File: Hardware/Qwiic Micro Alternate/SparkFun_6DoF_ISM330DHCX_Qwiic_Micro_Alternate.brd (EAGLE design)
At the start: 19.1 x 7.6 mm, 38 parts, among them J1 Qwiic Right Angle, U1 ISM330DHCX

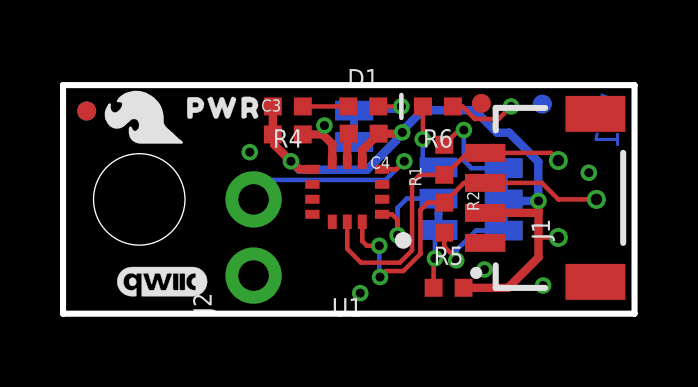
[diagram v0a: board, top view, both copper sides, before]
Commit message: Removes unused size
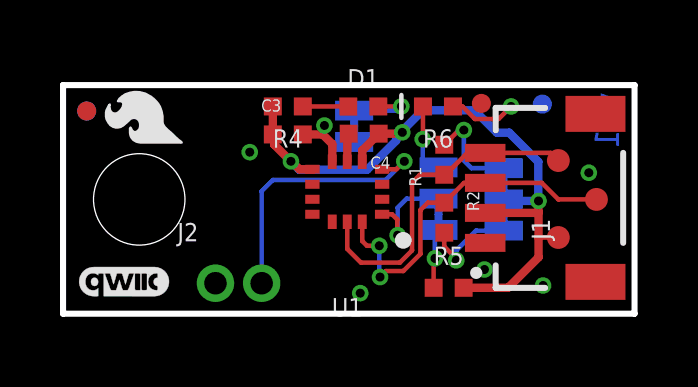
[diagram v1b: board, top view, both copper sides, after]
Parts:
- removed U$28: (no value), top:PWR8
- J2: device SparkFun-Connectors:1X02_NO_SILK -> SparkFun-Connectors:1X02_1.5MM_NO_SILK
- TP1, TP2, TP3: value TEST-POINTTP_15TH_THRU -> TEST-POINT3; device SparkFun-Connectors:TP_15TH -> SparkFun-Connectors:PAD.03X.03
- moved J2 1.30 mm to (5.08, 1.02), turned to 0 degrees
- moved LOGO1 1.27 mm to (2.03, 1.07)
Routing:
- net INT1: track 6.40 -> 9.08 mm
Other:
- board text removed: "Units in Inches"
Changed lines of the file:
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@@
 <drawing>
 <settings>
-<setting alwaysvectorfont="no"/>
+<setting alwaysvectorfont="yes"/>
 <setting keepoldvectorfont="yes"/>
 <setting verticaltext="up"/>
 </settings>
-<grid distance="0.05" unitdist="inch" unit="inch" style="dots" multiple="1" display="yes" altdistance="0.005" altunitdist="inch" altunit="inch"/>
+<grid distance="0.02" unitdist="inch" unit="inch" style="dots" multiple="1" display="yes" altdistance="0.005" altunitdist="inch" altunit="inch"/>
 <layers>
-<layer number="1" name="Top" color="4" fill="1" visible="yes" active="yes"/>
+<layer number="1" name="Top" color="4" fill="1" visible="no" active="yes"/>
 <layer number="2" name="Route2" color="1" fill="3" visible="no" active="no"/>
 <layer number="3" name="Route3" color="4" fill="3" visible="no" active="no"/>
@@
 <layer number="14" name="Route14" color="1" fill="6" visible="no" active="no"/>
 <layer number="15" name="Route15" color="4" fill="6" visible="no" active="no"/>
-<layer number="16" name="Bottom" color="3" fill="1" visible="yes" active="yes"/>
+<layer number="16" name="Bottom" color="3" fill="1" visible="no" active="yes"/>
 <layer number="17" name="Pads" color="26" fill="1" visible="yes" active="yes"/>
-<layer number="18" name="Vias" color="2" fill="1" visible="yes" active="yes"/>
+<layer number="18" name="Vias" color="2" fill="1" visible="no" active="yes"/>
 <layer number="19" name="Unrouted" color="6" fill="1" visible="yes" active="yes"/>
 <layer number="20" name="Dimension" color="15" fill="1" visible="yes" active="yes"/>
 <layer number="21" name="tPlace" color="16" fill="1" visible="yes" active="yes"/>
-<layer number="22" name="bPlace" color="14" fill="1" visible="yes" active="yes"/>
+<layer number="22" name="bPlace" color="14" fill="1" visible="no" active="yes"/>
 <layer number="23" name="tOrigins" color="15" fill="1" visible="yes" active="yes"/>
 <layer number="24" name="bOrigins" color="15" fill="1" visible="yes" active="yes"/>
@@
 <layer number="29" name="tStop" color="7" fill="3" visible="no" active="yes"/>
 <layer number="30" name="bStop" color="7" fill="6" visible="no" active="yes"/>
-<layer number="31" name="tCream" color="7" fill="4" visible="no" active="yes"/>
+<layer number="31" name="tCream" color="7" fill="4" visible="yes" active="yes"/>
 <layer number="32" name="bCream" color="7" fill="5" visible="no" active="yes"/>
 <layer number="33" name="tFinish" color="6" fill="3" visible="no" active="yes"/>
@@
 <layer number="37" name="tTest" color="7" fill="1" visible="no" active="yes"/>
 <layer number="38" name="bTest" color="7" fill="1" visible="no" active="yes"/>
-<layer number="39" name="tKeepout" color="4" fill="11" visible="no" active="yes"/>
+<layer number="39" name="tKeepout" color="4" fill="11" visible="yes" active="yes"/>
 <layer number="40" name="bKeepout" color="1" fill="11" visible="no" active="yes"/>
 <layer number="41" name="tRestrict" color="4" fill="10" visible="no" active="yes"/>
@@
 <layer number="45" name="Holes" color="7" fill="1" visible="yes" active="yes"/>
 <layer number="46" name="Milling" color="3" fill="1" visible="no" active="yes"/>
-<layer number="47" name="Measures" color="7" fill="1" visible="no" active="yes"/>
+<layer number="47" name="Measures" color="7" fill="1" visible="yes" active="yes"/>
 <layer number="48" name="Document" color="7" fill="1" visible="no" active="yes"/>
 <layer number="49" name="Reference" color="13" fill="1" visible="yes" active="yes"/>
 <layer number="50" name="dxf" color="7" fill="1" visible="no" active="no"/>
-<layer number="51" name="tDocu" color="6" fill="1" visible="yes" active="yes"/>
+<layer number="51" name="tDocu" color="6" fill="1" visible="no" active="yes"/>
 <layer number="52" name="bDocu" color="7" fill="1" visible="no" active="yes"/>
 <layer number="53" name="tGND_GNDA" color="7" fill="9" visible="no" active="no"/>
@@
 <text x="18.532475" y="7.375525" size="0.8128" layer="16" font="vector" ratio="22" rot="SMR270">v01</text>
 <dimension x1="14.0716" y1="3.8608" x2="13.97" y2="0" x3="22.86" y3="1.9304" textsize="1.778" textratio="15" layer="47" dtype="vertical" unit="inch"/>
-<text x="-1.27" y="-3.81" size="1.778" layer="47" font="vector" ratio="15">Units in Inches</text>
 <rectangle x1="9.1948" y1="4.953" x2="9.2456" y2="5.1816" layer="41"/>
 <dimension x1="19.05" y1="8.89" x2="0" y2="8.89" x3="9.525" y3="15.24" textsize="1.778" layer="47" dtype="horizontal" unit="inch"/>
 <dimension x1="2.54" y1="3.81" x2="0" y2="3.81" x3="1.27" y3="11.43" textsize="1.778" layer="47" dtype="horizontal" unit="inch"/>
-<dimension x1="0" y1="8.89" x2="0" y2="0" x3="-11.43" y3="4.445" textsize="1.778" layer="47" dtype="horizontal" unit="inch"/>
 <wire x1="18.542" y1="6.353175" x2="16.637" y2="6.353175" width="0.254" layer="22"/>
 <wire x1="17.145" y1="5.845175" x2="17.145" y2="6.988175" width="0.254" layer="22" curve="180"/>
@@
 <wire x1="3.190875" y1="7.24535" x2="2.784475" y2="5.63245" width="0.254" layer="22" curve="100"/>
 <circle x="3.6449" y="6.28015" radius="0.5334" width="0.254" layer="22"/>
-<dimension x1="2.54" y1="3.81" x2="2.54" y2="0" x3="-6.35" y3="1.905" textsize="1.778" layer="47" unit="inch"/>
 <wire x1="4.064" y1="5.842" x2="3.175" y2="6.731" width="0.254" layer="22"/>
 <wire x1="3.302" y1="5.842" x2="4.191" y2="6.731" width="0.254" layer="22"/>
+<dimension x1="0" y1="7.62" x2="0" y2="0" x3="-5.08" y3="3.81" textsize="1.778" layer="47" unit="inch"/>
 </plain>
 <attributes>
@@
 </element>
 <element name="U$25" library="bot" package="#I2C#11" value="" x="16.2814" y="3.8862" smashed="yes" rot="MR90"/>
-<element name="U$28" library="top" package="PWR8" value="" x="5.3594" y="6.858" smashed="yes"/>
 <element name="R5" library="SparkFun-Resistors" package="0402-TIGHT" value="10k" x="12.8524" y="0.8636" smashed="yes">
 <attribute name="NAME" x="12.8524" y="1.6256" size="0.6096" layer="25" font="vector" ratio="20" align="bottom-center"/>
@@
 <attribute name="VALUE" x="17.3736" y="2.2098" size="0.6096" layer="27" font="vector" ratio="20" rot="R90"/>
 </element>
-<element name="LOGO1" library="SparkFun-Aesthetics" package="QWIIC_3MM" value="QWIIC_LOGO_3MM" x="3.302" y="1.0668" smashed="yes"/>
+<element name="LOGO1" library="SparkFun-Aesthetics" package="QWIIC_3MM" value="QWIIC_LOGO_3MM" x="2.032" y="1.0668" smashed="yes"/>
 <element name="LOGO3" library="SparkFun-Aesthetics" package="BLANK" value="SFE_LOGO_NAME_FLAMEBLANK" x="-39.37" y="-15.24" smashed="yes"/>
-<element name="J2" library="SparkFun-Connectors" package="1X02_NO_SILK" value="" x="6.35" y="1.27" smashed="yes" rot="R90">
-<attribute name="NAME" x="4.953" y="0" size="0.6096" layer="25" font="vector" ratio="20" rot="R90"/>
-<attribute name="VALUE" x="8.382" y="0" size="0.6096" layer="27" font="vector" ratio="20" rot="R90"/>
+<element name="J2" library="SparkFun-Connectors" package="1X02_1.5MM_NO_SILK" value="" x="5.08" y="1.016" smashed="yes">
+<attribute name="NAME" x="3.81" y="2.413" size="0.6096" layer="25" font="vector" ratio="20"/>
+<attribute name="VALUE" x="3.81" y="-1.016" size="0.6096" layer="27" font="vector" ratio="20"/>
 </element>
 <element name="U$4" library="ISMTopMini" package="#INT1#112" value="" x="8.6106" y="3.7846" smashed="yes" rot="MR0"/>
@@
 <element name="U$3" library="ISMTopMini" package="#LED#2121" value="" x="7.3406" y="6.35" smashed="yes" rot="MR0"/>
 <element name="U$6" library="ISMTopMini" package="ISM330DHCX2120" value="" x="4.826" y="3.8354" smashed="yes" rot="MR90"/>
-<element name="TP1" library="SparkFun-Connectors" package="TP_15TH" value="TEST-POINTTP_15TH_THRU" x="16.51" y="5.1054" smashed="yes"/>
-<element name="TP2" library="SparkFun-Connectors" package="TP_15TH" value="TEST-POINTTP_15TH_THRU" x="17.78" y="3.81" smashed="yes"/>
-<element name="TP3" library="SparkFun-Connectors" package="TP_15TH" value="TEST-POINTTP_15TH_THRU" x="16.51" y="2.54" smashed="yes"/>
+<element name="TP1" library="SparkFun-Connectors" package="PAD.03X.03" value="TEST-POINT3" x="16.51" y="5.1054" smashed="yes"/>
+<element name="TP2" library="SparkFun-Connectors" package="PAD.03X.03" value="TEST-POINT3" x="17.78" y="3.81" smashed="yes"/>
+<element name="TP3" library="SparkFun-Connectors" package="PAD.03X.03" value="TEST-POINT3" x="16.51" y="2.54" smashed="yes"/>
 </elements>
 <signals>
@@
 <via x="11.37525" y="5.08" extent="1-16" drill="0.3"/>
 <wire x1="11.37525" y1="5.08" x2="10.75295" y2="4.4577" width="0.1524" layer="16"/>
-<wire x1="6.9977" y1="4.4577" x2="6.35" y2="3.81" width="0.1524" layer="16"/>
 <wire x1="10.75295" y1="4.4577" x2="6.9977" y2="4.4577" width="0.1524" layer="16"/>
+<wire x1="6.9977" y1="4.4577" x2="6.62" y2="4.08" width="0.1524" layer="16"/>
+<wire x1="6.62" y1="4.08" x2="6.62" y2="1.016" width="0.1524" layer="16"/>
 </signal>
 <signal name="3.3V">
